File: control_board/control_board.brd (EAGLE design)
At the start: 63 x 73.3 mm, 67 parts, among them IC1 ATMEGA1284P-MU, J1 USB Female Type C Connector, J5 20021311-00010T4LF, J6 20021311-00010T4LF, J7 20021311-00010T4LF, Q2 BSS84-7-F, Q3 BSS138PW,115, SW1 SPST_TACT-KMR2, U1 915MHz, U3 MCP73833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

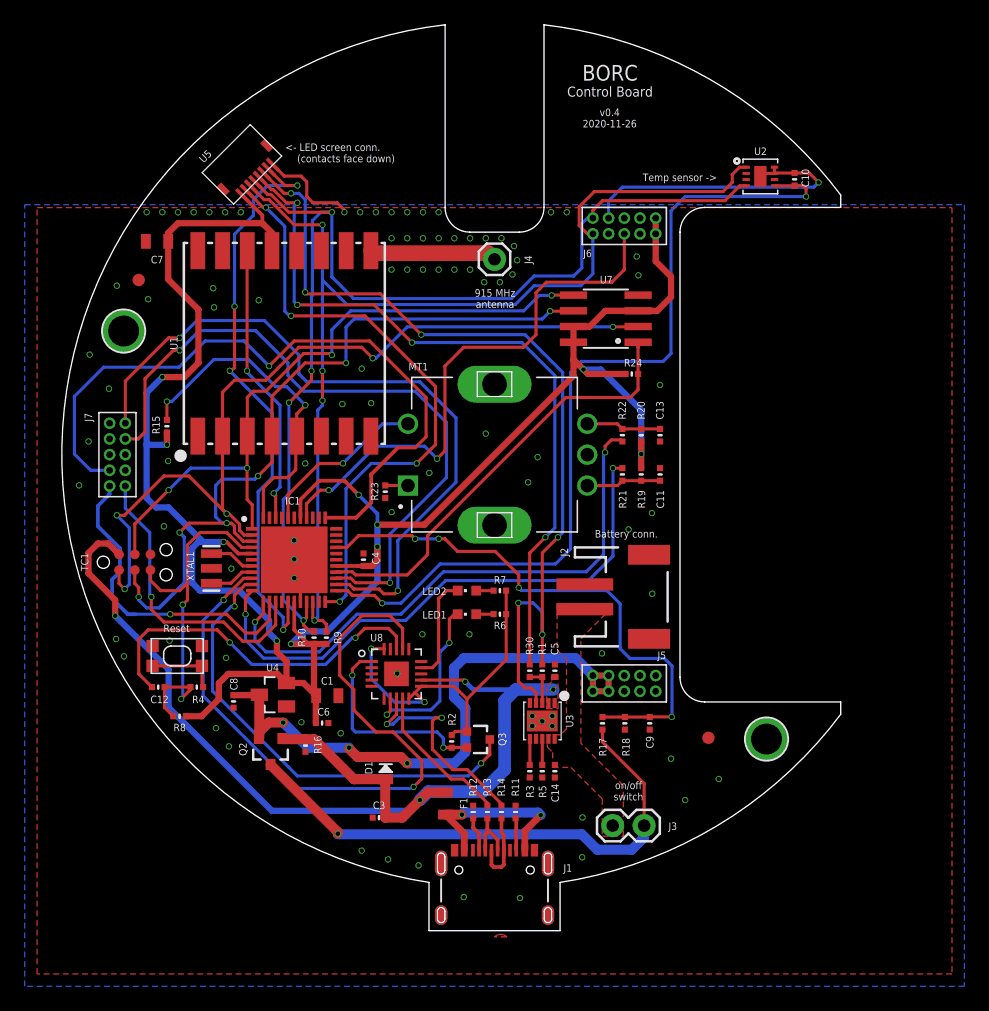
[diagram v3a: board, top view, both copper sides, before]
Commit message: v0.5 - major revision
- Replaced charger with smaller one (lower current consumption)
- Added power and charge LEDs
- wired red, green and blue LEDs
- replaced 12V sense with VBUS sense (current sensor monitors voltage as well)
- minor trace fixes
- updated gerbers and renders
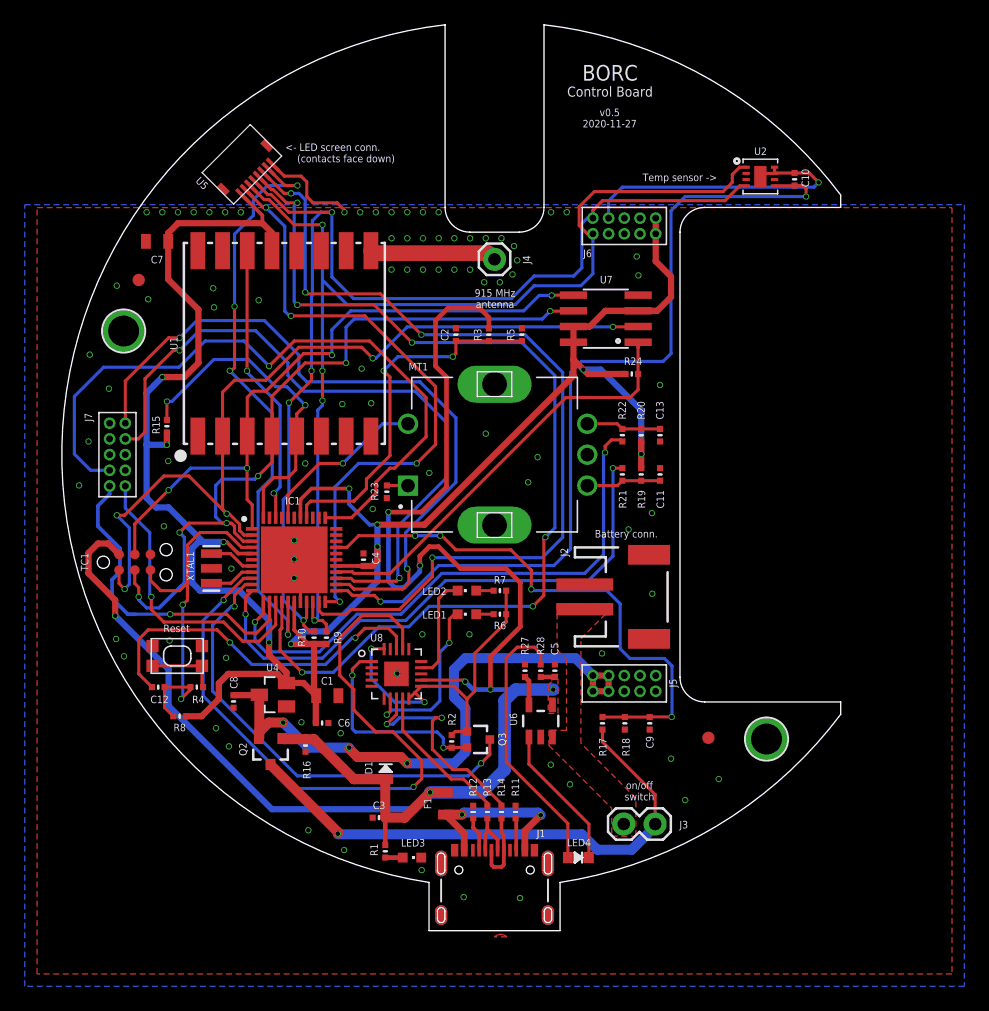
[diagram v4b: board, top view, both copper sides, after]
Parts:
- removed C14: 10uF, Adafruit Feather 32u4 Bluefruit LE:MICROBUILDER__0402MP
- removed R30: 330, Adafruit Feather 32u4 Bluefruit LE:MICROBUILDER__0402MP
- removed U3: MCP73833, SparkFun-IC-Power:DFN-10
- added C2: 0.1uF, Adafruit Feather 32u4 Bluefruit LE:MICROBUILDER__0402MP
- added LED3: PWR, adafruit:CHIPLED_0603
- added LED4: LED0603, LowPowerLab:0603-LED
- added R27: 2K, Adafruit Feather 32u4 Bluefruit LE:MICROBUILDER__0402MP
- added R28: 1K, Adafruit Feather 32u4 Bluefruit LE:MICROBUILDER__0402MP
- added U6: MCP73831, SparkFun:SOT23-5
- R1: value 330 -> 1K
- R3: value 1K -> 10M
- R5: value 10K -> 10M
- moved R3 35.5 mm to (34.5, 44.7), turned to 90 degrees
- moved R5 35.3 mm to (37.2, 44.7), turned to 90 degrees
- moved R1 19.4 mm to (26.2, 2.92), turned to 270 degrees
- moved J3 0.90 mm to (48.0, 5.13)
- moved R23 0.13 mm to (26.3, 32.0)
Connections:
- removed net 12V_SENSE: IC1.37, J6.5
- removed net CHARGE: R1.1, R30.1, U3.P$3
- removed net PROG: R3.1, U3.P$6
- removed net THERM: R5.1, U3.P$8
- new net N$16: LED4.PLUS, R28.1
- new net N$19: LED4.MINUS, U6.1
- new net N$2: LED3.A, R1.2
- new net PROG1: R27.1, U6.5
- new net VBUS_SENSE: C2.1, IC1.37, R3.1, R5.1
- net GND: now also C2.2, LED3.C, R27.2, U6.2; no longer C14.1, R3.2, U3.P$11, U3.P$5
- net GREEN: now also IC1.21; no longer R1.2, U3.P$4
- net RED: now also IC1.15; no longer R30.2
- net VBAT_CHG: now also U6.3; no longer C14.2, U3.P$10, U3.P$9
- net VBUS: now also R1.1, R28.2, R3.2, U6.4; no longer U3.P$1, U3.P$2
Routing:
- net VBUS: track 89.8 -> 147.7 mm, vias 4 -> 7
- net 12V_SENSE: track 44.4 -> 0.00 mm, vias 2 -> 0
- net VBUS_SENSE: track 0.00 -> 29.7 mm, vias 0 -> 2
- net RED: track 59.7 -> 82.3 mm, vias 4 -> 6
- net N$16: track 0.00 -> 22.5 mm
- net N$19: track 0.00 -> 11.8 mm
- net CHARGE: track 3.12 -> 0.00 mm
- net PROG1: track 0.00 -> 2.39 mm
- net PROG: track 2.11 -> 0.00 mm
- net THERM: track 2.11 -> 0.00 mm
- net N$2: track 0.00 -> 1.41 mm
- net CS: track 35.5 -> 34.5 mm
- net SDB: track 49.8 -> 50.7 mm
- net TEMP: track 57.3 -> 56.5 mm
- net BLUE: track 47.7 -> 48.5 mm
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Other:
- board text added: "v0.5 2020-11-27"
- board text removed: "v0.4 2020-11-26"

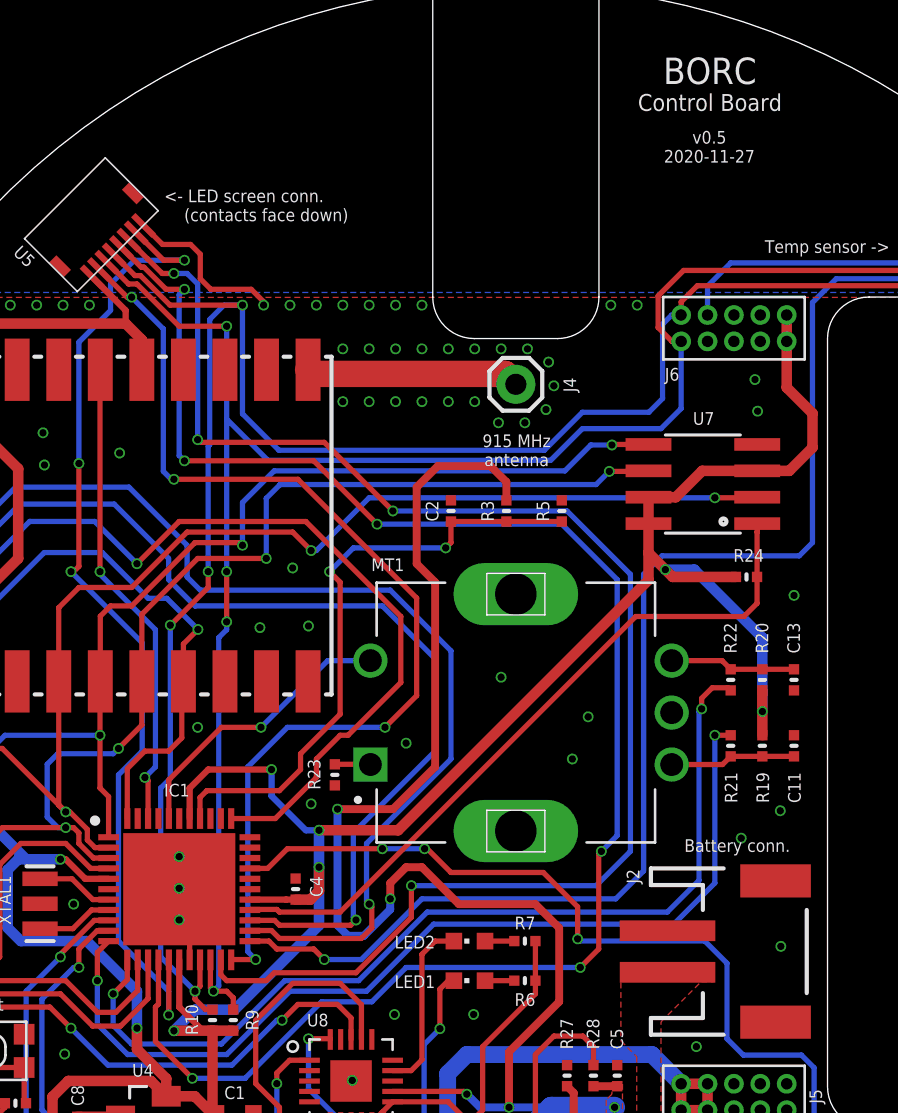
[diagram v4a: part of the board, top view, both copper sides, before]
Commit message: v0.6 - control board design update
- changed green pin to a PWM pin
- Added driver power control pin
- updated gerbers, render, schematic
- ERC/DRC
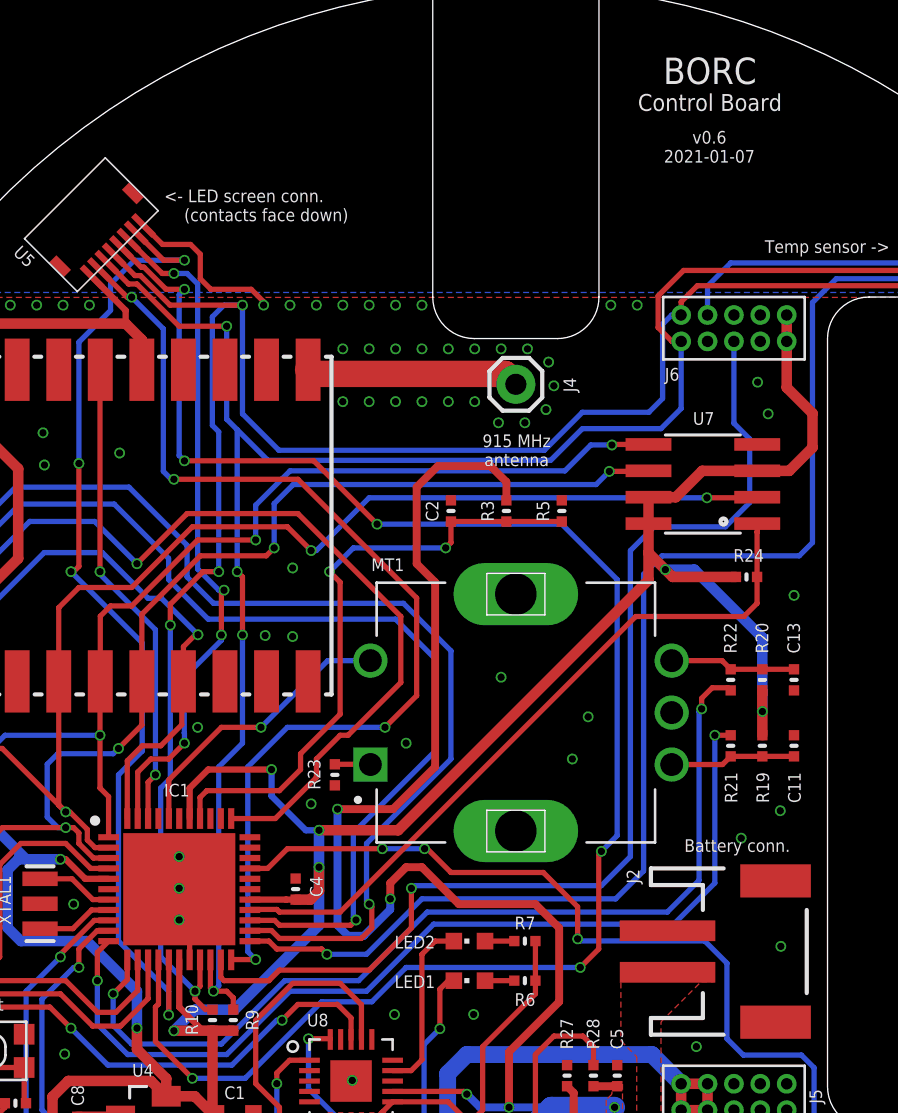
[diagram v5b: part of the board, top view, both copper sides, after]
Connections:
- new net DRIVER_POWER: IC1.21, J6.5
- net GREEN: now also IC1.43; no longer IC1.21
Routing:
- net DRIVER_POWER: track 0.00 -> 53.7 mm, vias 0 -> 1
- net GREEN: track 72.5 -> 32.8 mm
- net SCL: track 91.8 -> 92.5 mm
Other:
- board text added: "v0.6 2021-01-07"
- board text removed: "v0.5 2020-11-27"

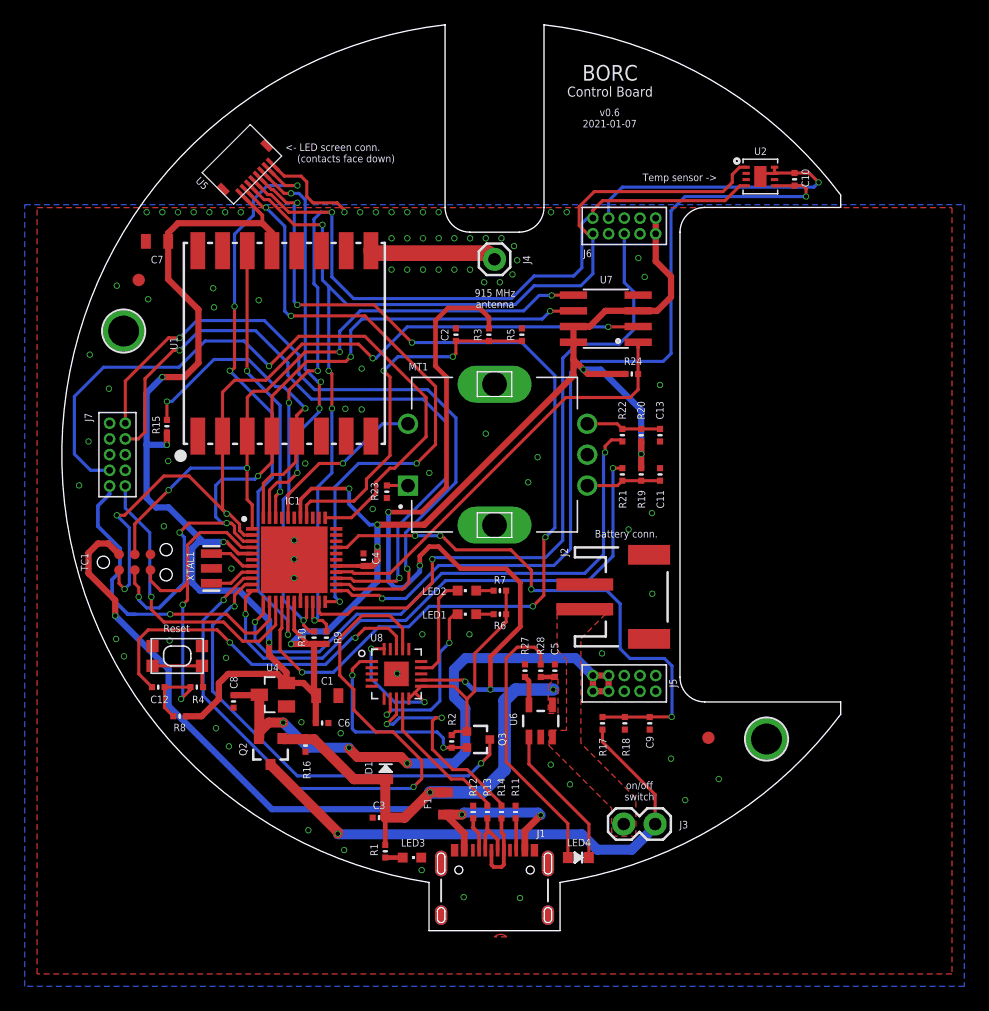
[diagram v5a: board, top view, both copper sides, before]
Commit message: v0.7 - control board update
- Added pull up resistor to SHT31 ADDR pin (address changed from 0x44 to 0x45)
- Added cutout to control board to allow power board to be screwed from top
- Added cutout to FPC connector
- Rearranged some traces and components - slight adjustments
- gerbers updated
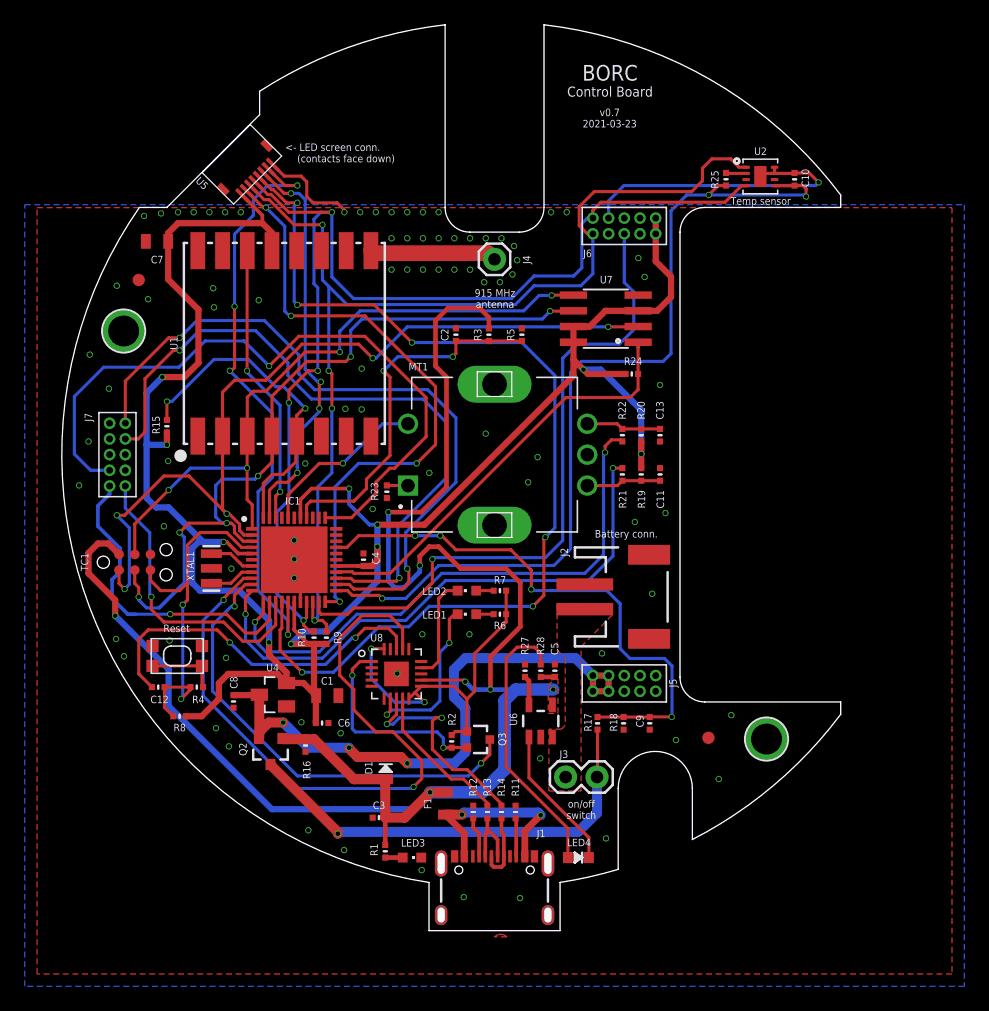
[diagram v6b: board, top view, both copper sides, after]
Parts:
- added R25: 10K, Adafruit Feather 32u4 Bluefruit LE:MICROBUILDER__0402MP
- C1, C7: value 10µF -> 0.33µF
- F1: value 10V 1.5A -> 6V 0.5A
- J1: device SparkFun-Connectors:USB-C-16P -> SparkFun-Connectors:USB-C-16P-2LAYER-PADS
- moved J3 6.04 mm to (43.3, 8.93)
- moved R17 0.40 mm to (43.3, 13.3)
- moved R18 0.10 mm to (45.4, 13.3)
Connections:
- new net N$20: R25.2, U2.2
- net TEMP_SENSOR_POWER: now also R25.1
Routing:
- net VBAT: track 44.5 -> 36.3 mm
- net TEMP_SENSOR_POWER: track 70.2 -> 72.0 mm, vias 2 -> 3
- net N$20: track 0.00 -> 1.64 mm
- net N$7: track 4.69 -> 5.68 mm
- net N$10: track 14.7 -> 15.7 mm
- net SDA: track 87.5 -> 88.3 mm
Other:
- outline, holes or cut-outs redrawn
- board text added: "Temp sensor"
- board text added: "v0.7 2021-03-23"
- board text removed: "Temp sensor ->"
- board text removed: "v0.6 2021-01-07"
